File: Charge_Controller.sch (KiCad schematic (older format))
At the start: 16 parts

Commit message: Initial Schematic capture DRAFT
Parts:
- added C1, C11, C13, C20, C3, C4: 100nf, symbol Device:C_Small
- added C10: 10uf, symbol Device:CP
- added C14, C16: 100uf, symbol Device:CP
- added C15, C17: 33nf, symbol Device:C_Small
- added C18, C21, C22, C5, C6: 4.7uf, symbol Device:CP
- added C2, C9: 2.2uf, symbol Device:C_Small
- added C6: 4.7uf, symbol Device:C_Small
- added C7, C8: 470uf, symbol Device:CP
- added D1, D2, D3: SS310, symbol Device:D_Schottky
- added D4, D8: 1N4007, Diode_THT:D_DO-41_SOD81_P10.16mm_Horizontal, symbol Diode:1N4007
- added D5, D6, D7: D_Schottky, symbol Device:D_Schottky
- added F1, F2: 35A, symbol Device:Fuse
- added J?: USB_OTG, symbol Connector:USB_OTG
- added J? (x29): Conn_01x01_Female, symbol Connector:Conn_01x01_Female
- added J?: SOLAR, symbol Connector:Conn_01x02_Male
- added J?: BATT, symbol Connector:Conn_01x02_Male
- added L1, L2, L3: 100uH, symbol pspice:INDUCTOR
- added LED2: LED, symbol Device:LED
- added Q1, Q2, Q3: CSD19505, Package_TO_SOT_THT:TO-220-3_Vertical, symbol Device:Q_NMOS_GDS
- added Q4: Si2306, symbol Device:Q_NMOS_DGS
- added Q5, Q6: 2N3904, Package_TO_SOT_THT:TO-92_Inline, symbol Transistor_BJT:2N3904
- added R1: 200k, symbol Device:R
- added R10, R9: 100, symbol Device:R
- added R11, R8: 100k, symbol Device:R
- added R13, R20, R22, R23, R31, R37, R4, R6, R7: 10k, symbol Device:R
- added R14, R15, R17, R18: 15k, symbol Device:R
- added R16, R19, R34, R5: 1k, symbol Device:R
- added R2: 5.1k, symbol Device:R
- added R3: 3.3k, symbol Device:R
- added R32, R33: 47k, symbol Device:R
- added R? (x2): 0R, symbol Device:R
- added U1: ACS712-30A, Package_SO:SOIC-8_3.9x4.9mm_P1.27mm, symbol Sensor_Current:ACS712xLCTR-30A
- added U10: ADS1015, Package_SO:TSSOP-10_3x3mm_P0.5mm, symbol Analog_ADC:ADS1015IDGS
- added U2: B1212, Converter_DCDC:Converter_DCDC_muRata_CRE1xxxxxxSC_THT, symbol Regulator_Switching:CRE1S1212SC
- added U3: AMS1117-5.0, Package_TO_SOT_SMD:SOT-223-3_TabPin2, symbol Regulator_Linear:AMS1117-3.3
- added U4: AMS1117-3.3, Package_TO_SOT_SMD:SOT-223-3_TabPin2, symbol Regulator_Linear:AMS1117-3.3
- added U5, U6: XL7005A, Package_SO:SOIC-8_3.9x4.9mm_P1.27mm, symbol Regulator_Switching:GL2576-3.3SF8DR
- added U7: IR2104, symbol Driver_FET:IR2104
- added U9: CH340G, Package_SO:SOIC-16_3.9x9.9mm_P1.27mm, symbol Interface_USB:CH340G
- gave numbers to parts that had none: 1
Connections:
- net +3V3: now also R24.2, C20.2, D7.1 (K), R31.2, U10.8 (VDD), U9.16 (VCC), U9.4 (V3); no longer R24.1
- net EN: now also Q5.3 (C)
- net GND: now also C1.2, C11.1, C13.2, C14.2, C16.2, C18.2, C2.1, C20.1, C21.2, C22.2, C5.2, C6.1, C6.2, C7.2, C8.2, C9.2, D5.2 (A), D6.2 (A), J?.1 (Pin_1), J?.1 (Pin_1), J?.2 (Pin_2), J?.2 (Pin_2), J?.5 (GND), J?.6 (Shield), Q3.3 (S), Q4.3 (S), R11.2, R13.1, R16.1, R19.1, R2.2, R20.1, R34.2, R4.2, R7.2, R?.1, R?.1, U1.5 (GND), U10.1 (ADDR), U10.3 (GND), U3.1 (GND), U4.1 (GND), U5.5 (GND), U5.6 (GND), U5.7 (GND), U5.8 (GND), U6.5 (GND), U6.6 (GND), U6.7 (GND), U6.8 (GND), U7.4 (COM), U9.1 (GND)
- net at U8.10 (IO25): now also J?.1 (Pin_1)
- net at U8.11 (IO26): now also J?.1 (Pin_1)
- net GPIO27: now reaches U8.12 (IO27)
- net GPIO27: now also Q4.2 (G), R7.1
- net at U8.13 (IO14): now also J?.1 (Pin_1)
- net at U8.14 (IO12): now also J?.1 (Pin_1)
- net at U8.16 (IO13): now also J?.1 (Pin_1)
- net at U8.17 (SHD/SD2): now also J?.1 (Pin_1)
- net at U8.18 (SWP/SD3): now also J?.1 (Pin_1)
- net at U8.19 (SCS/CMD): now also J?.1 (Pin_1)
- net at U8.20 (SCK/CLK): now also J?.1 (Pin_1)
- net at U8.21 (SDO/SD0): now also J?.1 (Pin_1)
- net at U8.22 (SDI/SD1): now also J?.1 (Pin_1)
- net at U8.23 (IO15): now also J?.1 (Pin_1)
- net GPIO0: now reaches U8.25 (IO0)
- net GPIO0: now also R24.1; no longer R24.2
- net at U8.26 (IO4): now also J?.1 (Pin_1)
- net GPIO17: now reaches U8.27 (IO16)
- net GPIO17: now also R28.2, U8.28 (IO17)
- net at U8.29 (IO5): now also J?.1 (Pin_1)
- net GPIO18: now reaches R27.2, U8.30 (IO18)
- net GPIO19: now reaches R26.2, U8.31 (IO19)
- net SDA: now reaches R30.2, U8.33 (IO21)
- net SDA: now also U10.9 (SDA)
- net RX: now reaches U8.34 (RXD0/IO3)
- net RX: now also U9.3 (RXD)
- net TX: now reaches U8.35 (TXD0/IO1)
- net TX: now also U9.2 (TXD)
- net SCL: now reaches R29.2, U8.36 (IO22)
- net SCL: now also U10.10 (SCL)
- net at U8.4 (SENSOR_VP): now also J?.1 (Pin_1)
- net at U8.5 (SENSOR_VN): now also J?.1 (Pin_1)
- net GPIO34: now reaches U8.6 (IO34)
- net GPIO34: now also R31.1, U10.2 (ALERT/RDY)
- net GPIO32: now reaches U8.8 (IO32)
- net GPIO32: now also R20.2, U7.3 (~SD)
- net GPIO33: now reaches U8.9 (IO33)
- net GPIO33: now also R13.2, U7.2 (IN)
- new net: J?.1 (Pin_1), U9.10 (~DSR)
- new net: J?.1 (Pin_1), U9.11 (~RI)
- new net: J?.1 (Pin_1), U9.12 (~DCD)
- new net: Q6.1 (E), R22.1, U9.13 (~DTR)
- new net: Q5.1 (E), R23.2, U9.14 (~RTS)
- new net: J?.1 (Pin_1), U9.15 (R232)
- new net: J?.3 (D+), U9.5 (UD+)
- new net: J?.2 (D-), U9.6 (UD-)
- new net: J?.1 (Pin_1), U9.7 (XI)
- new net: J?.1 (Pin_1), U9.8 (XO)
- new net: J?.1 (Pin_1), U9.9 (~CTS)
- new net: C22.1, D7.2 (A), U4.2 (VO)
- new net: C21.1, J?.1 (VBUS), U4.3 (VI)
- new net: Q5.2 (B), R22.2
- new net: Q6.2 (B), R23.1
- new net: C18.1, D4.1 (K), D8.1 (K), U5.1 (VIN), U6.1 (VIN)
- new net: D5.1 (K), L2.1, U5.2 (VOUT)
- new net: C15.2, R14.2, R15.2, R16.2, U5.3 (FB)
- new net: R?.2, U5.4 (~ON~/OFF)
- new net: C4.2, Q4.1 (D), U2.1 (-VIN)
- new net: C3.2, LED2.1 (K), Q1.3 (S), R37.1, U1.3 (IP-), U1.4 (IP-), U2.3 (-VOUT)
- new net: C3.1, Q1.1 (G), R37.2, R6.2, U2.4 (+VOUT)
- new net: D6.1 (K), L3.1, U6.2 (VOUT)
- new net: C17.2, R17.2, R18.2, R19.2, U6.3 (FB)
- new net: R?.2, U6.4 (~ON~/OFF)
- new net: LED2.2 (A), R6.1
- new net: C10.2, L1.1, Q2.3 (S), Q3.2 (D), R8.2, U7.6 (VS)
- new net: C8.1, F2.2, L1.2, R32.1, R33.1
- new net: C7.1, F1.1, R1.1, U1.1 (IP+), U1.2 (IP+)
- new net: R3.1, U1.6 (FILTER)
- new net: C2.2, U1.7 (VIOUT)
- new net: D8.2 (A), F1.2, J?.1 (Pin_1)
- new net: D2.1 (K), R10.1, U7.5 (LO)
- new net: D1.1 (K), R9.1, U7.7 (HO)
- new net: C10.1, D3.1 (K), U7.8 (VB)
- new net: D4.2 (A), F2.1, J?.1 (Pin_1)
- new net: R3.2, R4.1, R5.2
- new net: Q1.2 (D), Q2.2 (D)
- new net: D2.2 (A), Q3.1 (G), R10.2, R11.1
- new net: D1.2 (A), Q2.1 (G), R8.1, R9.2
- new net 12V: C11.2, C14.1, C15.1, C4.1, C5.1, D3.2 (A), J?.1 (Pin_1), L2.2, R14.1, R15.1, U2.2 (+VIN), U3.3 (VI), U7.1 (VCC)
- new net 3.3V: C16.1, C17.1, J?.1 (Pin_1), L3.2, R17.1, R18.1
- new net 5.0V: C6.1, C6.2, J?.1 (Pin_1), U1.8 (VCC), U3.2 (VO)
- new net A0: J?.1 (Pin_1), U10.4 (AIN0)
- new net A1: C13.1, R32.2, R33.2, R34.1, U10.5 (AIN1)
- new net A2: C9.1, R5.1, U10.6 (AIN2)
- new net A3: C1.1, R1.2, R2.1, U10.7 (AIN3)
- new net IO0: Q6.3 (C)
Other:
- note added: "12V BUCK REGULATOR"
- note added: "3.3V BUCK REGULATOR"
- note added: "BACKFLOW CURRENT CONTROL UNIT\n(BCCU)"
- note added: "ESP32 MICROCONTROLLER"
- note added: "EXTERNAL 12BIT ADC"
- note added: "INPUT CURRENT SENSORS"
- note added: "INPUT VOLTAGE DIVIDER"
- note added: "SYNCHRONOUS\nBUCK"
- note added: "USB-TTL USART (ESP 32 USB PROGRAMMER)"
- moved on the sheet: C12, C19, C23, LED1, R12, R21, R24, R25, R26, R27, R28, R29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

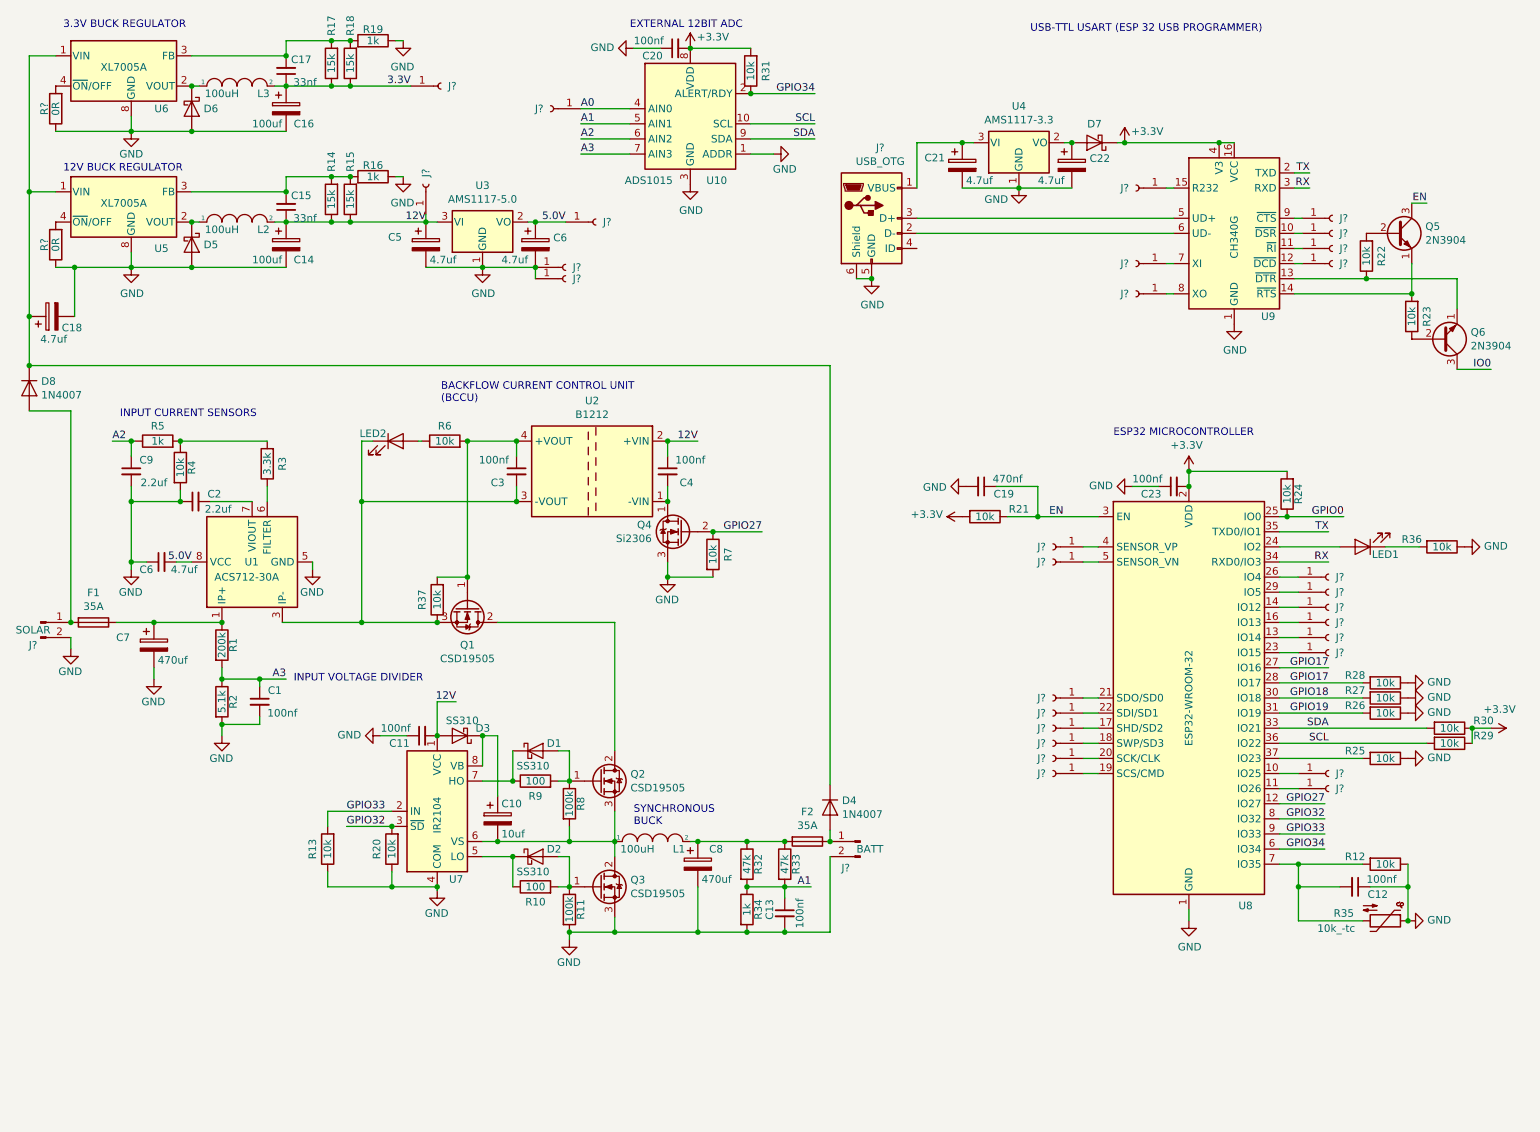
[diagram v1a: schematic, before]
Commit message: Draft BOM, ADDED surge and reverse polarity protection U11, Q7, Q8
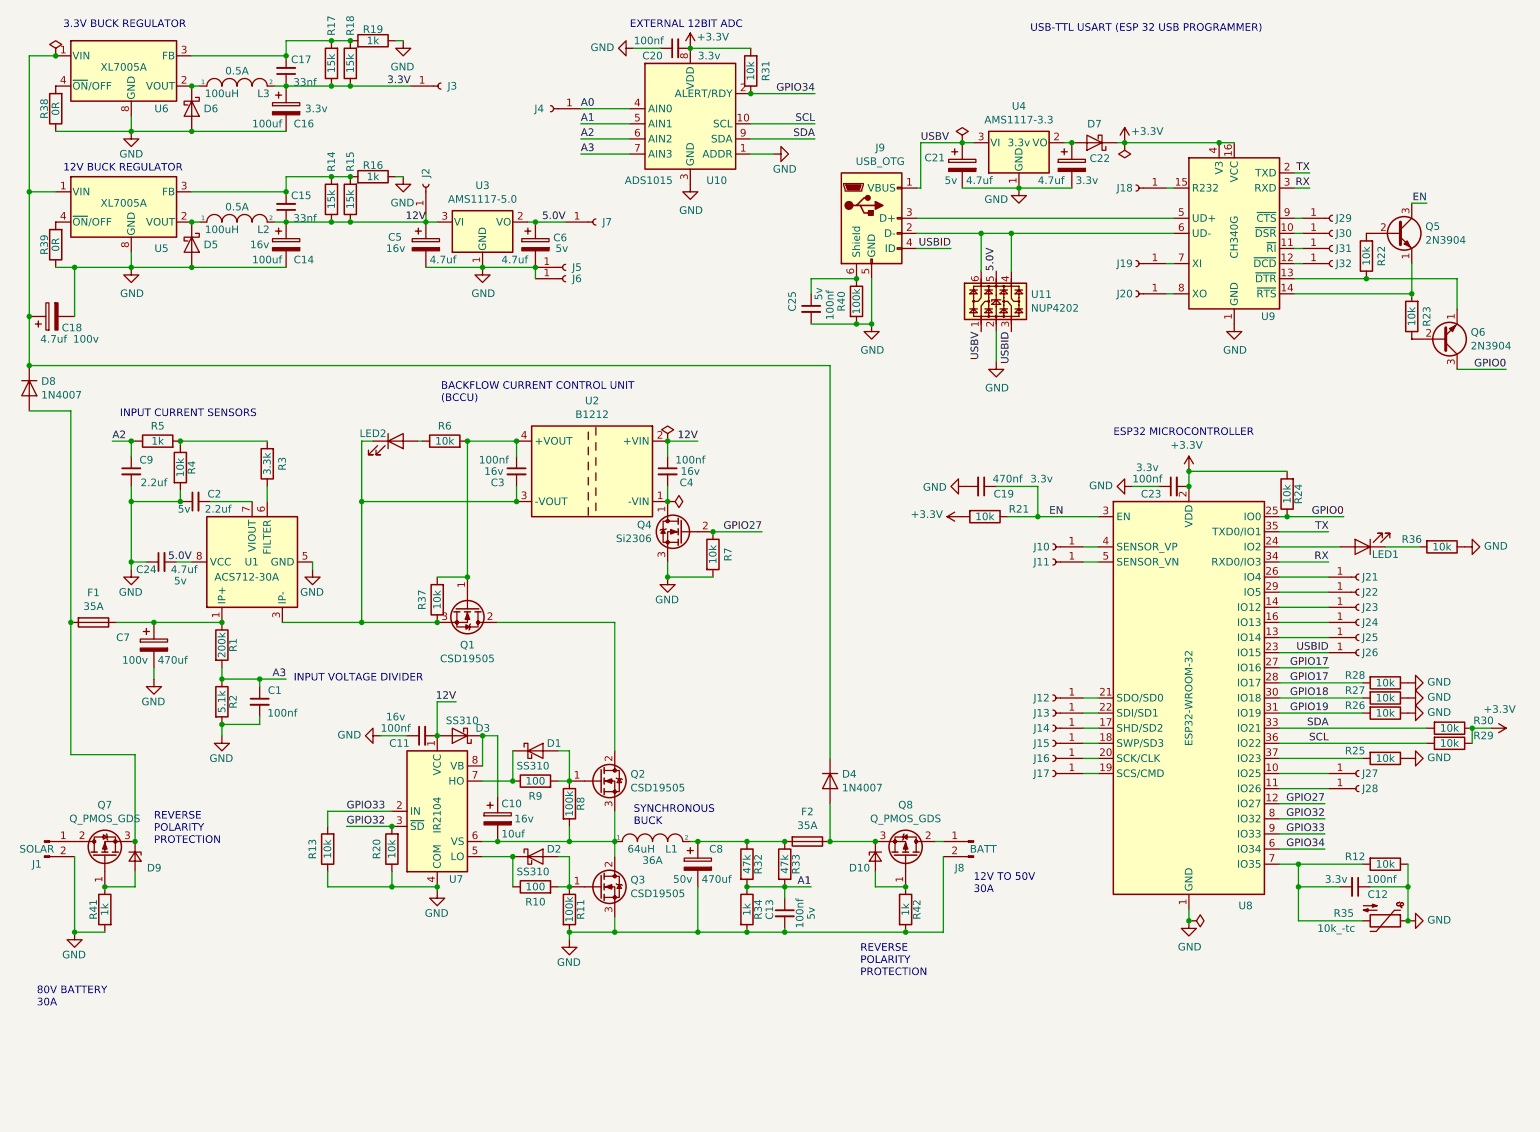
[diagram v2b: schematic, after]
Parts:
- added C25: 100nf, Capacitor_SMD:C_0805_2012Metric, symbol Device:C_Small
- added D10, D9: D_Zener_Small, symbol Device:D_Zener_Small
- added Q7, Q8: Q_PMOS_GDS, symbol Device:Q_PMOS_GDS
- added R40: 100k, Resistor_SMD:R_0805_2012Metric, symbol Device:R
- added R41, R42: 1k, Resistor_SMD:R_0805_2012Metric, symbol Device:R
- added U11: NUP4202, Package_TO_SOT_SMD:SOT-363_SC-70-6, symbol Power_Protection:NUP4202
- C1, C13: footprint (none) -> Capacitor_SMD:C_0805_2012Metric; Field4 (none) -> 5v; jlcpcb (none) -> C28233
- C10: footprint (none) -> Capacitor_SMD:C_0805_2012Metric; Field4 (none) -> 16v; jlcpcb (none) -> C15850
- C11, C3, C4: footprint (none) -> Capacitor_SMD:C_0805_2012Metric; Field4 (none) -> 16v; jlcpcb (none) -> C28233
- C12, C20, C23: footprint (none) -> Capacitor_SMD:C_0805_2012Metric; Field4 (none) -> 3.3v; jlcpcb (none) -> C28233
- C14: footprint (none) -> Capacitor_SMD:CP_Elec_8x10; Field4 (none) -> 16v; jlcpcb (none) -> C445063
- C15, C17: footprint (none) -> Capacitor_SMD:C_0805_2012Metric; Field4 (none) -> 5v; jlcpcb (none) -> C53175
- C16: footprint (none) -> Capacitor_SMD:CP_Elec_8x10; Field4 (none) -> 3.3v; jlcpcb (none) -> C445063
- C18: footprint (none) -> Capacitor_THT:CP_Radial_D10.0mm_P5.00mm; Digikey (none) -> 399-ESH107M100AH4AA-ND; Field4 (none) -> 100v; jlcpcb (none) -> NA
- C19: footprint (none) -> Capacitor_SMD:C_0805_2012Metric; Field4 (none) -> 3.3v; jlcpcb (none) -> C13967
- C2: footprint (none) -> Capacitor_SMD:C_0805_2012Metric; Field4 (none) -> 5v; jlcpcb (none) -> C49217
- C21, C6: footprint (none) -> Capacitor_SMD:C_0805_2012Metric; Field4 (none) -> 5v; jlcpcb (none) -> C1779
- C22: footprint (none) -> Capacitor_SMD:C_0805_2012Metric; Field4 (none) -> 3.3v; jlcpcb (none) -> C1779
- C24: renamed from C6; footprint (none) -> Capacitor_SMD:C_0805_2012Metric; Field4 (none) -> 5v; jlcpcb (none) -> C1779
- C5: footprint (none) -> Capacitor_SMD:C_0805_2012Metric; Field4 (none) -> 16v; jlcpcb (none) -> C1779
- C7: footprint (none) -> Capacitor_THT:CP_Axial_L30.0mm_D18.0mm_P35.00mm_Horizontal; Digikey (none) -> 4100PHBK-ND; Field4 (none) -> 100v; jlcpcb (none) -> NA
- C8: footprint (none) -> Capacitor_THT:CP_Axial_L30.0mm_D18.0mm_P35.00mm_Horizontal; Digikey (none) -> 4100PHBK-ND; Field4 (none) -> 50v; jlcpcb (none) -> NA
- C9: footprint (none) -> Capacitor_SMD:C_0805_2012Metric; jlcpcb (none) -> C49217
- D1, D2, D3: footprint (none) -> Diode_SMD:D_SMA; jlcpcb (none) -> C15874
- D4, D8: footprint Diode_THT:D_DO-41_SOD81_P10.16mm_Horizontal -> Diode_SMD:D_SMA; jlcpcb (none) -> C727081
- D5, D6, D7: value D_Schottky -> SS310; footprint (none) -> Diode_SMD:D_SMA; jlcpcb (none) -> C15874
- F1, F2: footprint (none) -> Fuse:Fuseholder_Blade_Mini_Keystone_3568; Digikey (none) -> 36-3568-10-ND; jlcpcb (none) -> NA
- J10, J11, J12, J13, J14, J15, J16, J17, J18, J19, J2, J20, J21, J22, J23, J24, J25, J26, J27, J28, J29, J3, J30, J31, J32, J4, J5, J6, J7: renamed from J?; footprint (none) -> TestPoint:TestPoint_Loop_D3.50mm_Drill0.9mm_Beaded
- J9: renamed from J?; footprint (none) -> Connector_USB:USB_Micro-AB_Molex_47590-0001; jlcpcb (none) -> C136001
- L1: value 100uH -> 64uH; Field4 (none) -> 36A
- L2, L3: footprint (none) -> Inductor_SMD:L_Taiyo-Yuden_NR-60xx_HandSoldering; Field4 (none) -> 0.5A; jlcpcb (none) -> C88132
- LED1, LED2: footprint (none) -> LED_SMD:LED_0805_2012Metric; jlcpcb (none) -> C84256
- Q1, Q2, Q3: jlcpcb (none) -> C485534
- Q4: footprint (none) -> Package_TO_SOT_SMD:SOT-23; jlcpcb (none) -> C347489
- Q5, Q6: footprint Package_TO_SOT_THT:TO-92_Inline -> Package_TO_SOT_SMD:SOT-23; jlcpcb (none) -> C18536
- R1: footprint (none) -> Resistor_SMD:R_0805_2012Metric; jlcpcb (none) -> C17539
- R10, R9: footprint (none) -> Resistor_SMD:R_0805_2012Metric; jlcpcb (none) -> C17408
- R11, R8: footprint (none) -> Resistor_SMD:R_0805_2012Metric; jlcpcb (none) -> C149504
- R12, R13, R20, R21, R22, R23, R24, R25, R26, R27, R28, R29, R30, R31, R36, R37, R4, R6, R7: footprint (none) -> Resistor_SMD:R_0805_2012Metric; jlcpcb (none) -> C17724
- R14, R15, R17, R18: footprint (none) -> Resistor_SMD:R_0805_2012Metric; jlcpcb (none) -> C17475
- R16, R19, R34, R5: footprint (none) -> Resistor_SMD:R_0805_2012Metric; jlcpcb (none) -> C17513
- R2: footprint (none) -> Resistor_SMD:R_0805_2012Metric; jlcpcb (none) -> C27834
- R3: footprint (none) -> Resistor_SMD:R_0805_2012Metric; jlcpcb (none) -> C26010
- R32, R33: footprint (none) -> Resistor_SMD:R_0805_2012Metric; jlcpcb (none) -> C17713
- R38, R39: renamed from R?; footprint (none) -> Resistor_SMD:R_0603_1608Metric; jlcpcb (none) -> C21189
- U1: jlcpcb (none) -> C9932
- U10: jlcpcb (none) -> C193969
- U2: jlcpcb (none) -> C5127060
- U3: Field4 (none) -> 5.0v; jlcpcb (none) -> C6187
- U4: Field4 (none) -> 3.3v; jlcpcb (none) -> C6186
- U5, U6: jlcpcb (none) -> C50848
- U7: footprint (none) -> Package_SO:SOIC-8_3.9x4.9mm_P1.27mm; jlcpcb (none) -> C2960
- U8: jlcpcb (none) -> C701343
- U9: jlcpcb (none) -> C14267
- gave numbers to parts that had none: 2
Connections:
- net IO0 is gone; now on net GPIO0: Q6.3 (C)
- net 5.0V: now also U11.5
- net GND: now also C25.2, R40.2, R41.2, R42.2, U11.2; no longer J9.6 (Shield)
- net USBID: now reaches J26.1 (Pin_1), U8.23 (IO15)
- net USBID: now also J9.4 (ID), U11.3
- net at J9.2 (D-), U9.6 (UD-): now also U11.4, U11.6
- net USBV: now reaches C21.1, J9.1 (VBUS), U4.3 (VI)
- net USBV: now also U11.1
- net at D8.2 (A), F1.2: now also D9.1 (K), Q7.3 (S); no longer J1.1 (Pin_1)
- net at D4.2 (A), F2.1: now also D10.1 (K), Q8.3 (S); no longer J8.1 (Pin_1)
- new net: C25.1, J9.6 (Shield), R40.1
- new net: J1.1 (Pin_1), Q7.2 (D)
- new net: J8.1 (Pin_1), Q8.2 (D)
- new net: D10.2 (A), Q8.1 (G), R42.1
- new net: D9.2 (A), Q7.1 (G), R41.1
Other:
- note added: "12V TO 50V\n30A"
- note added: "80V BATTERY\n30A"
- note added: "REVERSE \nPOLARITY\nPROTECTION"
- moved on the sheet: D4, J1, J21, J22, J23, J24, J25, J26, J27, J28, J8

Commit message: Aligned footprints with JLPCB rotations and offsets, deleted some JLCPCB automation files.
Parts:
- added J33: SOLAR, TestPoint:TestPoint_Keystone_5005-5009_Compact, symbol Connector:Conn_01x01_Male
- added J34: BATT, TestPoint:TestPoint_Keystone_5005-5009_Compact, symbol Connector:Conn_01x01_Male
- D10, D9: footprint (none) -> Diode_SMD:D_MELF-RM10_Universal_Handsoldering; jlcpcb (none) -> C8062
- J1, J8: footprint (none) -> TestPoint:TestPoint_Keystone_5005-5009_Compact; symbol Connector:Conn_01x02_Male -> Connector:Conn_01x01_Male; Digikey (none) -> 277-13746-ND; jlcpcb (none) -> NA
- J10, J11, J12, J13, J14, J15, J16, J17, J18, J19, J2, J20, J21, J22, J23, J24, J25, J26, J27, J28, J29, J3, J30, J31, J32, J4, J5, J6, J7: jlcpcb (none) -> NA
- L1: footprint (none) -> Inductor_THT:L_Axial_L30.0mm_D8.0mm_P35.56mm_Horizontal_Fastron_77A; jlcpcb (none) -> NA
- Q7, Q8: value Q_PMOS_GDS -> PMOS-100V-90A; footprint (none) -> Package_TO_SOT_SMD:TO-263-2; jlcpcb (none) -> C468007
- R35: footprint (none) -> Connector_PinHeader_1.00mm:PinHeader_1x02_P1.00mm_Vertical; Digikey (none) -> BC2380-ND; jlcpcb (none) -> NA
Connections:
- net GND: now also J33.1 (Pin_1), J34.1 (Pin_1); no longer J1.2 (Pin_2), J8.2 (Pin_2)
